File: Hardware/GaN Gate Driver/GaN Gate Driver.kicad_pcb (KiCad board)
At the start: 2 copper layers, 38.1 x 38.1 mm, 24 parts, among them J1 3296W-1-102LF, U1 LT1804

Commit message: Updating gate driver board
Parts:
- removed R7: 10k, Resistor_SMD:R_0805_2012Metric
- added C6: 1uF, Capacitor_SMD:C_0805_2012Metric, F.Cu at (53.3, 38.1)
- added C7: 1uF, Capacitor_SMD:C_0805_2012Metric, F.Cu at (53.3, 50.8)
- added J2: Conn_01x03_Socket, Connector_PinSocket_2.54mm:PinSocket_1x03_P2.54mm_Vertical, F.Cu at (53.3, 41.9)
- added J3: Conn_01x02_Socket, Connector_PinSocket_2.54mm:PinSocket_1x02_P2.54mm_Vertical, F.Cu at (68.6, 60.3)
- added R10: 10k, Resistor_SMD:R_0805_2012Metric, F.Cu at (76.8, 37.5)
- added R11: 0, Resistor_SMD:R_0805_2012Metric, F.Cu at (83.8, 37.5)
- added R12: 10k, Resistor_SMD:R_0805_2012Metric, F.Cu at (76.8, 40.0)
- added R13: 500, Resistor_SMD:R_0805_2012Metric, F.Cu at (83.8, 42.5)
- added R8: 10k, Resistor_SMD:R_0805_2012Metric, F.Cu at (83.8, 34.9)
- added R9: 10k, Resistor_SMD:R_0805_2012Metric, F.Cu at (76.8, 34.9)
- J1: value 3296W-1-102LF -> SMA-J-P-X-ST-EM1
- R4: value 50 -> 47
- RV1: value R_Potentiometer_US -> 3296W-1-102LF
- moved TP1 106.5 mm to (43.8, 33.0)
- moved TP2 106.5 mm to (43.8, 36.1)
- moved TP3 106.5 mm to (43.8, 39.1)
- moved C2 88.1 mm to (58.4, 36.0)
- moved C3 83.6 mm to (62.9, 36.2)
- moved D1 75.5 mm to (62.9, 48.3)
- moved C4 75.2 mm to (71.8, 48.3)
- moved C5 74.7 mm to (71.8, 43.8)
- moved C1 73.5 mm to (73.0, 32.4)
- moved R1 70.9 mm to (62.9, 41.3)
- moved R6 70.5 mm to (62.9, 38.7)
- moved R5 70.2 mm to (62.9, 43.8)
- moved R2 66.4 mm to (67.3, 43.8)
- moved R3 64.6 mm to (68.6, 32.4)
- moved R4 56.2 mm to (76.8, 42.5)
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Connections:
- R4 pad 1: Net-(J1-In) -> Net-(R4-Pad1)
- U1 pad 5: GND -> Net-(U1B-+)
- U1 pad 7: Net-(U1B--) -> Net-(R4-Pad1)

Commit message: Working on gate driver board
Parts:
- moved TP2 43.6 mm to (83.2, 54.6)
- moved TP3 39.2 mm to (82.5, 45.1)
- moved TP1 33.8 mm to (62.9, 61.0)
- moved R13 13.4 mm to (71.8, 48.3)
- moved C2 11.8 mm to (67.3, 43.8)
- moved C4 11.7 mm to (62.9, 40.6)
- moved R8 10.3 mm to (76.8, 42.5)
- moved C3 7.01 mm to (62.2, 43.2)
- moved R9 5.08 mm to (76.8, 40.0)
- moved R5 4.84 mm to (58.4, 45.7)
- moved R2 4.45 mm to (67.3, 48.3)
- moved R1 3.17 mm to (62.9, 38.1)
- moved R6 3.17 mm to (62.9, 35.6)
- moved R10 2.54 mm to (76.8, 34.9)
- moved R12 2.54 mm to (76.8, 37.5)
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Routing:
- net Net-(U1A--): track 0.00 -> 31.8 mm, vias 0 -> 1
- net Net-(D1-A): track 0.00 -> 23.6 mm
- net Net-(J1-In): track 0.00 -> 21.8 mm
- net Net-(U1B-+): track 0.00 -> 21.1 mm
- net Net-(C4-Pad1): track 0.00 -> 20.2 mm
- net Net-(J3-Pin_1): track 0.00 -> 20.2 mm
- net Net-(U1A-+): track 0.00 -> 15.8 mm
- net Net-(R4-Pad1): track 0.00 -> 15.0 mm
- net +5V: track 0.00 -> 11.2 mm
- net -5V: track 0.00 -> 8.69 mm
- net Net-(U1B--): track 0.00 -> 6.66 mm

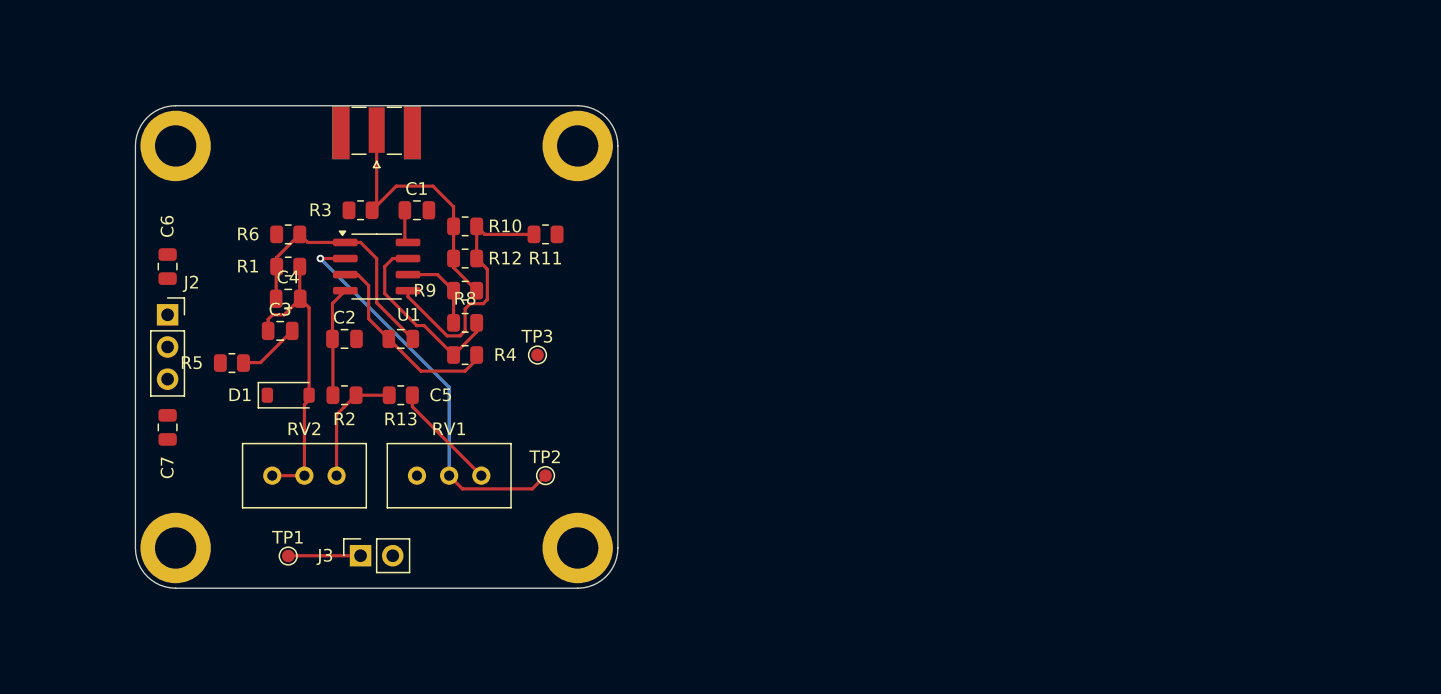
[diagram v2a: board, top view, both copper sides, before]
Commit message: Updating board layout
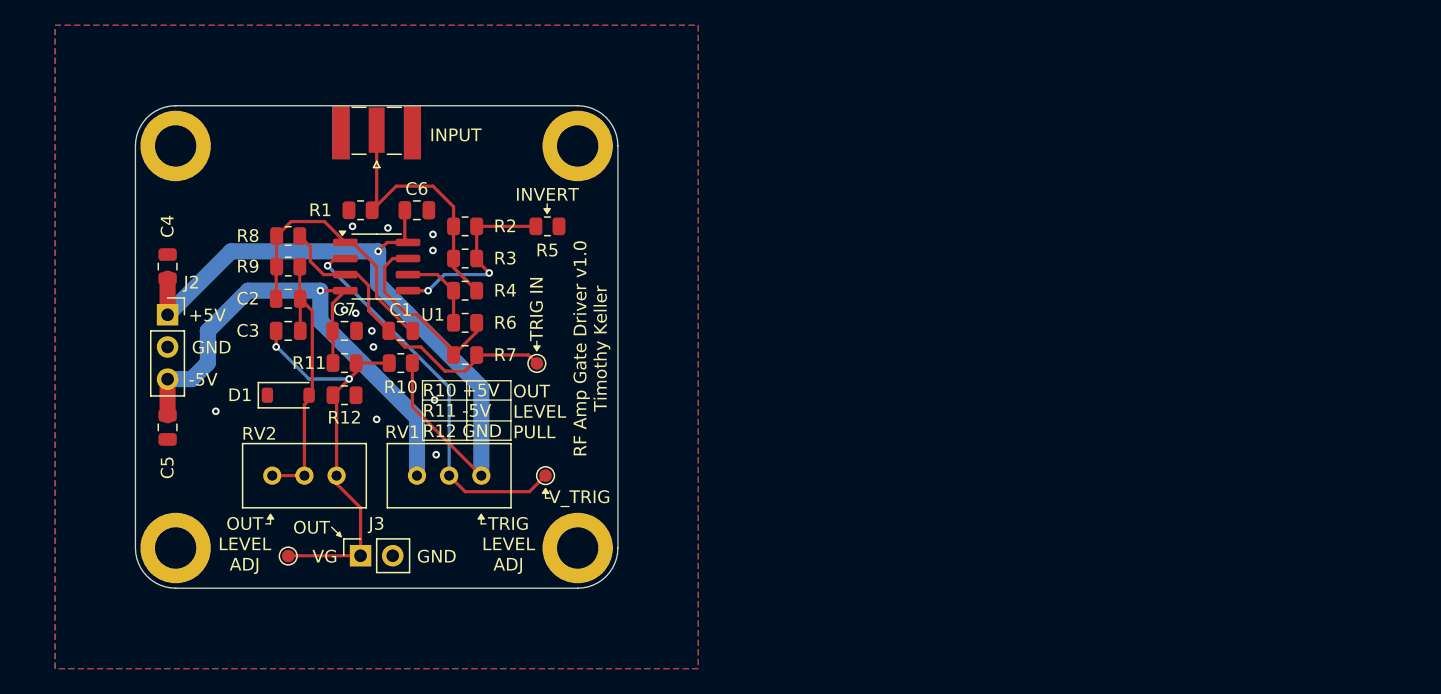
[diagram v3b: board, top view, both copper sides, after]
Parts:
- moved R12 9.25 mm to (67.3, 48.3), turned to 180 degrees
- moved R10 2.54 mm to (71.8, 45.7)
- moved R11 2.54 mm to (67.3, 45.7)
- moved TP1 0.67 mm to (82.5, 45.8)
- moved R5 0.65 mm to (83.3, 34.9)
- moved C3 0.64 mm to (62.9, 43.2), turned to 180 degrees
- moved C1 0.63 mm to (71.8, 43.2)
- moved C7 0.63 mm to (67.3, 43.2)
- moved R8 0.13 mm to (62.9, 35.7), turned to 180 degrees
- renumbered C5 to C1, C4 to C2, C6 to C4, C7 to C5, C1 to C6, C2 to C7, R3 to R1, R13 to R10, R2 to R11, R5 to R12, R10 to R2, R12 to R3, R9 to R4, R11 to R5, R8 to R6, R4 to R7, R6 to R8, R1 to R9, TP3 to TP1, TP1 to TP3
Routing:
- net +5V: track 11.2 -> 59.1 mm, vias 0 -> 1
- net -5V: track 8.69 -> 45.2 mm, vias 0 -> 1
- net Net-(J3-Pin_1): track 20.2 -> 33.1 mm, vias 0 -> 2
- net Net-(U1A-+): track 15.8 -> 26.0 mm
- net Net-(U1B-+): track 21.1 -> 15.8 mm, vias 0 -> 2
- net Net-(D1-A): track 23.6 -> 22.3 mm
- net Net-(C1-Pad2): track 20.2 -> 21.4 mm
- net Net-(U1A--): track 31.8 -> 30.8 mm
- net GND: vias 0 -> 12
- added copper zone on B.Cu, net GND
- added copper zone on F.Cu, net GND
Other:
- board text added: "${TITLE} ${REVISION} ${COMMENT1}"
- board text added: "+5V"
- board text added: "-5V"
- board text added: "GND"
- board text added: "INPUT"
- board text added: "INVERT"
- board text added: "OUT"
- board text added: "OUT LEVEL ADJ"
- board text added: "OUT LEVEL PULL"
- board text added: "R10 +5V R11 -5V R12 GND"
- board text added: "TRIG IN"
- board text added: "TRIG LEVEL ADJ"
- board text added: "VG"
- board text added: "V_TRIG"
